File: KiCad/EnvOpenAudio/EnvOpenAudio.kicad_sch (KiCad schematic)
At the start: 65 parts, among them J1 USB_C_Receptacle_USB2.0, J2 Button, J5 Conn_01x03_Male, U1 TLV75533PDBV, U2 LM3880, U3 RP2040, U4 TLV320AIC3100, U5 TLV75518PDBV, U6 TLV75533PDBV, Y1 3225_4P 12MHz

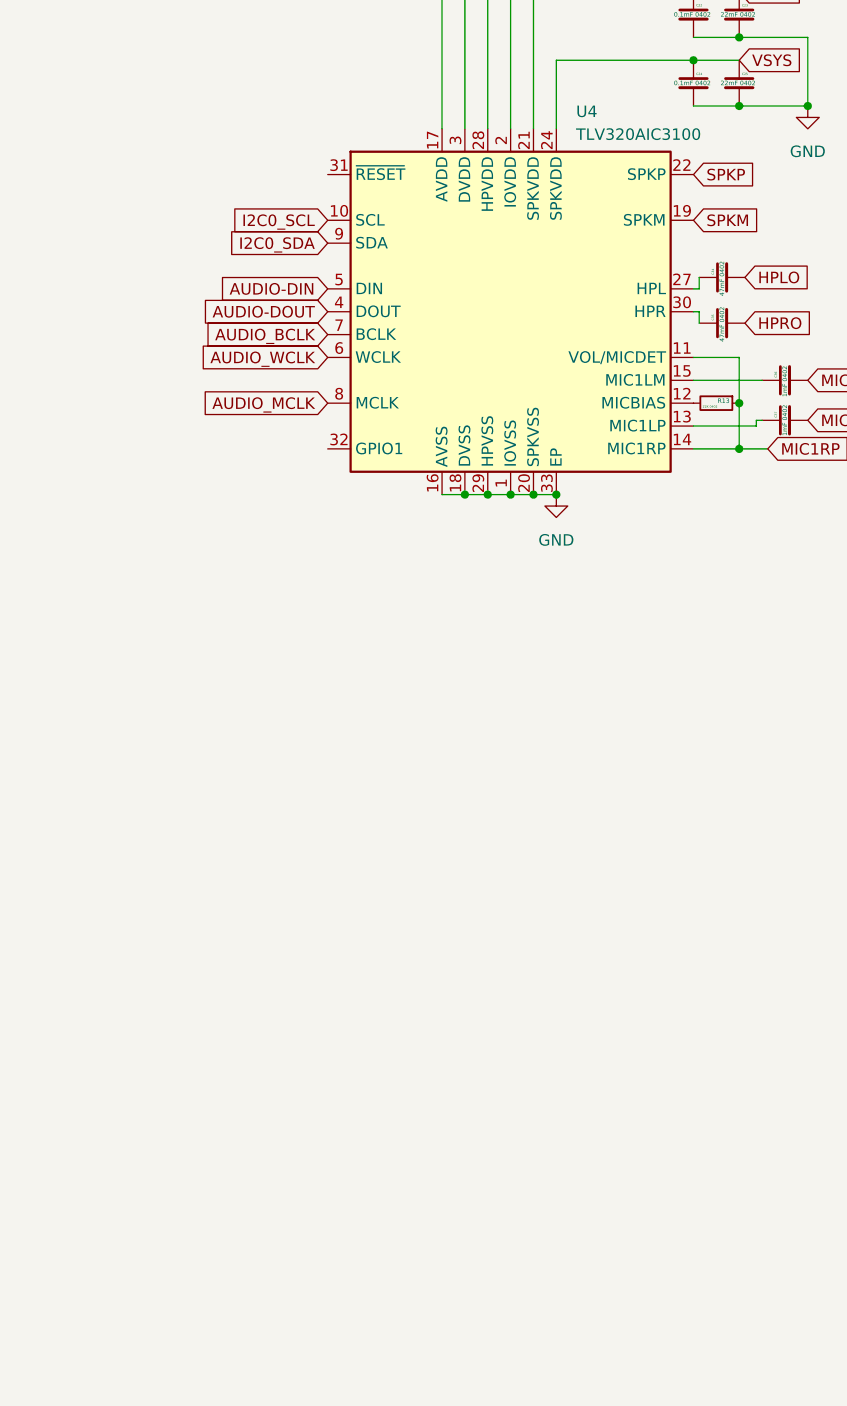
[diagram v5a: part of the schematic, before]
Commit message: wired up majority of PCB, added headers and labels.
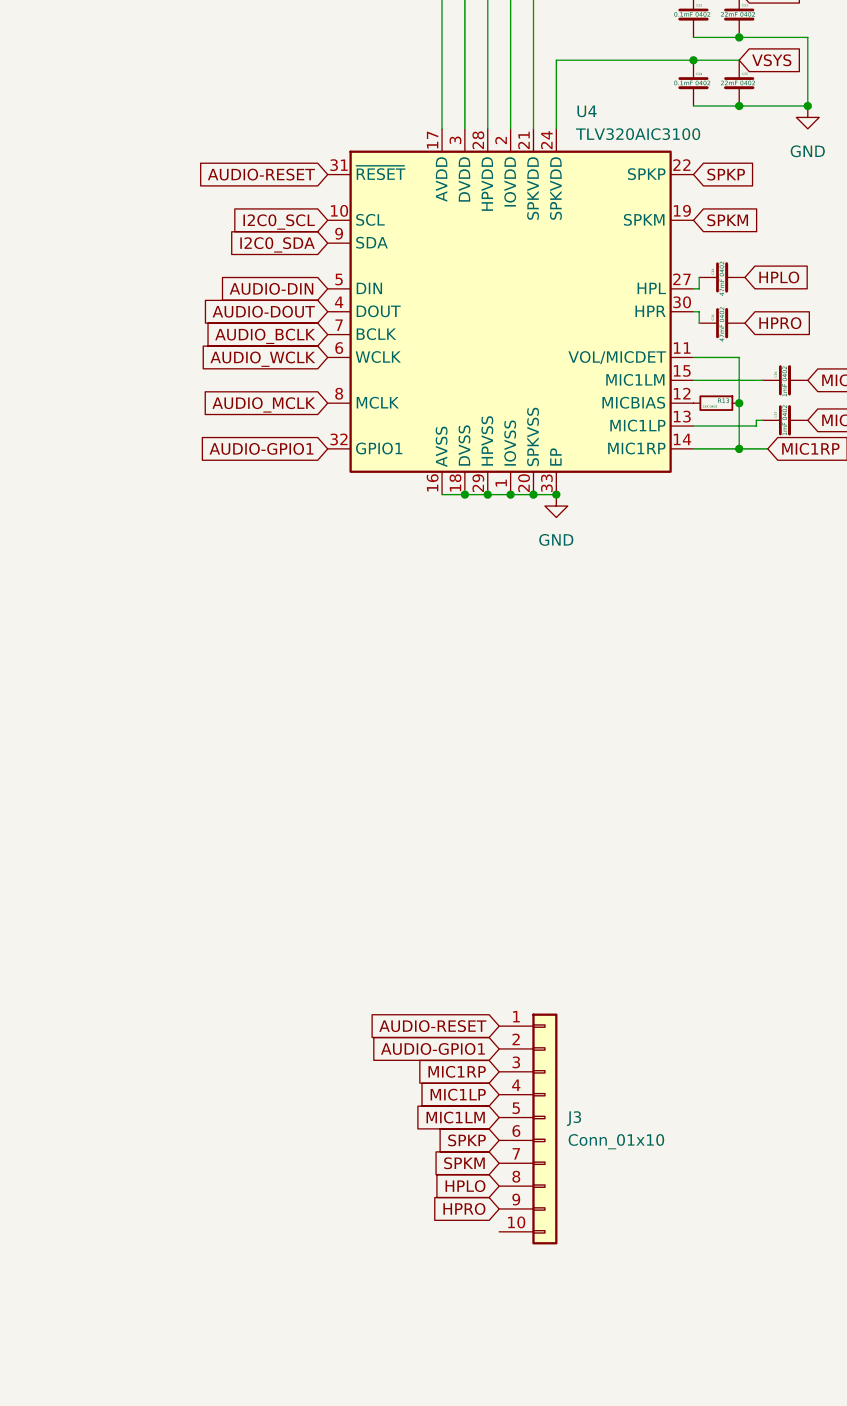
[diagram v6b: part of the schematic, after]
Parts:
- added J3: Conn_01x10, Connector_PinHeader_2.54mm:PinHeader_2x05_P2.54mm_Vertical, symbol Connector_Generic:Conn_01x10
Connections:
- net HPLO: now also J3.8 (Pin_8)
- net HPRO: now also J3.9 (Pin_9)
- net MIC1LM: now also J3.5 (Pin_5)
- net MIC1LP: now also J3.4 (Pin_4)
- net MIC1RP: now also J3.3 (Pin_3)
- net SPKM: now also J3.7 (Pin_7)
- net SPKP: now also J3.6 (Pin_6)
- net AUDIO-RESET: now reaches U4.31 (~{RESET})
- net AUDIO-RESET: now also J3.1 (Pin_1)
- net AUDIO-GPIO1: now reaches U4.32 (GPIO1)
- net AUDIO-GPIO1: now also J3.2 (Pin_2)
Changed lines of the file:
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@@
     (effects (font (size 1.27 1.27)) (justify right bottom))
   )
+  (global_label "AUDIO-RESET" (shape input) (at 311.15 186.055 180) (fields_autoplaced)
+    (effects (font (size 1.27 1.27)) (justify right))
+    (property "Intersheetrefs" "${INTERSHEET_REFS}" (at 295.8771 186.055 0)
+      (effects (font (size 1.27 1.27)) (justify right) hide)
+    )
+  )
   (global_label "USB_D-" (shape input) (at 43.18 34.925 0) (fields_autoplaced)
     (effects (font (size 1.27 1.27)) (justify left))
@@
     )
   )
+  (global_label "AUDIO-GPIO1" (shape input) (at 292.1 121.92 180) (fields_autoplaced)
+    (effects (font (size 1.27 1.27)) (justify right))
+    (property "Intersheetrefs" "${INTERSHEET_REFS}" (at 276.8874 121.92 0)
+      (effects (font (size 1.27 1.27)) (justify right) hide)
+    )
+  )
   (global_label "AUDIO_MCLK" (shape input) (at 292.1 116.84 180) (fields_autoplaced)
     (effects (font (size 1.27 1.27)) (justify right))
@@
     )
   )
+  (global_label "AUDIO-RESET" (shape input) (at 292.1 91.44 180) (fields_autoplaced)
+    (effects (font (size 1.27 1.27)) (justify right))
+    (property "Intersheetrefs" "${INTERSHEET_REFS}" (at 276.8271 91.44 0)
+      (effects (font (size 1.27 1.27)) (justify right) hide)
+    )
+  )
   (global_label "I2C0_SCL" (shape input) (at 292.1 96.52 180) (fields_autoplaced)
     (effects (font (size 1.27 1.27)) (justify right))
@@
     )
   )
+  (global_label "MIC1LM" (shape input) (at 311.15 196.215 180) (fields_autoplaced)
+    (effects (font (size 1.27 1.27)) (justify right))
+    (property "Intersheetrefs" "${INTERSHEET_REFS}" (at 301.8038 196.215 0)
+      (effects (font (size 1.27 1.27)) (justify right) hide)
+    )
+  )
   (global_label "AUDIO_MCLK" (shape input) (at 172.085 194.945 0) (fields_autoplaced)
     (effects (font (size 1.27 1.27)) (justify left))
@@
     )
   )
+  (global_label "MIC1RP" (shape input) (at 311.15 191.135 180) (fields_autoplaced)
+    (effects (font (size 1.27 1.27)) (justify right))
+    (property "Intersheetrefs" "${INTERSHEET_REFS}" (at 301.7433 191.135 0)
+      (effects (font (size 1.27 1.27)) (justify right) hide)
+    )
+  )
+  (global_label "MIC1LP" (shape input) (at 311.15 193.675 180) (fields_autoplaced)
+    (effects (font (size 1.27 1.27)) (justify right))
+    (property "Intersheetrefs" "${INTERSHEET_REFS}" (at 301.9852 193.675 0)
+      (effects (font (size 1.27 1.27)) (justify right) hide)
+    )
+  )
   (global_label "I2C0_SDA" (shape input) (at 172.085 189.865 0) (fields_autoplaced)
     (effects (font (size 1.27 1.27)) (justify left))
@@
     )
   )
+  (global_label "SPKM" (shape input) (at 311.15 201.295 180) (fields_autoplaced)
+    (effects (font (size 1.27 1.27)) (justify right))
+    (property "Intersheetrefs" "${INTERSHEET_REFS}" (at 303.6181 201.295 0)
+      (effects (font (size 1.27 1.27)) (justify right) hide)
+    )
+  )
   (global_label "VSYS" (shape input) (at 140.97 45.72 180) (fields_autoplaced)
     (effects (font (size 1.27 1.27)) (justify right))
@@
     )
   )
+  (global_label "HPLO" (shape input) (at 311.15 203.835 180) (fields_autoplaced)
+    (effects (font (size 1.27 1.27)) (justify right))
+    (property "Intersheetrefs" "${INTERSHEET_REFS}" (at 303.8599 203.835 0)
+      (effects (font (size 1.27 1.27)) (justify right) hide)
+    )
+  )
   (global_label "AUDIO_BCLK" (shape input) (at 292.1 109.22 180) (fields_autoplaced)
     (effects (font (size 1.27 1.27)) (justify right))
@@
     )
   )
+  (global_label "HPRO" (shape input) (at 311.15 206.375 180) (fields_autoplaced)
+    (effects (font (size 1.27 1.27)) (justify right))
+    (property "Intersheetrefs" "${INTERSHEET_REFS}" (at 303.618 206.375 0)
+      (effects (font (size 1.27 1.27)) (justify right) hide)
+    )
+  )
   (global_label "AUDIO-DIN" (shape input) (at 292.1 104.14 180) (fields_autoplaced)
     (effects (font (size 1.27 1.27)) (justify right))
@@
     )
   )
+  (global_label "AUDIO-GPIO1" (shape input) (at 311.15 188.595 180) (fields_autoplaced)
+    (effects (font (size 1.27 1.27)) (justify right))
+    (property "Intersheetrefs" "${INTERSHEET_REFS}" (at 295.9374 188.595 0)
+      (effects (font (size 1.27 1.27)) (justify right) hide)
+    )
+  )
   (global_label "AUDIO-DOUT" (shape input) (at 292.1 106.68 180) (fields_autoplaced)
     (effects (font (size 1.27 1.27)) (justify right))
@@
     (property "Intersheetrefs" "${INTERSHEET_REFS}" (at 344.7472 78.74 0)
       (effects (font (size 1.27 1.27)) (justify left) hide)
+    )
+  )
+  (global_label "SPKP" (shape input) (at 311.15 198.755 180) (fields_autoplaced)
+    (effects (font (size 1.27 1.27)) (justify right))
+    (property "Intersheetrefs" "${INTERSHEET_REFS}" (at 303.7995 198.755 0)
+      (effects (font (size 1.27 1.27)) (justify right) hide)
     )
   )
@@
         )
       )
+    )
+  )
+  (symbol (lib_id "Connector_Generic:Conn_01x10") (at 316.23 196.215 0) (unit 1)
+    (in_bom yes) (on_board yes) (dnp no) (fields_autoplaced)
+    (property "Reference" "J3" (at 318.77 196.215 0)
+      (effects (font (size 1.27 1.27)) (justify left))
+    )
+    (property "Value" "Conn_01x10" (at 318.77 198.755 0)
+      (effects (font (size 1.27 1.27)) (justify left))
+    )
+    (property "Footprint" "Connector_PinHeader_2.54mm:PinHeader_2x05_P2.54mm_Vertical" (at 316.23 196.215 0)
+      (effects (font (size 1.27 1.27)) hide)
+    )
+    (property "Datasheet" "~" (at 316.23 196.215 0)
+      (effects (font (size 1.27 1.27)) hide)
+    )
+    (pin "6")
+    (pin "10")
+    (pin "9")
+    (pin "3")
+    (pin "8")
+    (pin "4")
+    (pin "1")
+    (pin "5")
+    (pin "7")
+    (pin "2")
+    (instances
+      (project "EnvOpenAudio"
+        (path "/7b892ee5-f34f-4bca-8f87-a56522432f7c"
+          (reference "J3") (unit 1)
+        )
+      )

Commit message: Swapped RP2040 for RP2350A for FPU, re-did board and schematic, added labels back and naming, Github link
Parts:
- removed C1: 10uf 0402, Capacitor_SMD:C_0402_1005Metric, symbol Device:C
- removed C10: 2.2uF 0402, Capacitor_SMD:C_0402_1005Metric, symbol Device:C
- removed C16, C5, C6: 100nf 0402, Capacitor_SMD:C_0402_1005Metric, symbol Device:C
- removed C20, C21: 10uf 0402, Capacitor_SMD:C_0402_1005Metric, symbol Device:C_Small
- removed FLASH1: W25Q16JVUXIQ, Package_SON:SON-8-1EP_3x2mm_P0.5mm_EP1.4x1.6mm, symbol Memory_Flash:W25Q32JVZP
- removed J2: Button, Button_Switch_SMD:SW_SPST_B3U-1000P, symbol Switch:SW_Push
- removed J5: Conn_01x03_Male, Connector_PinHeader_1.00mm:PinHeader_1x03_P1.00mm_Vertical, symbol Connector_Generic:Conn_01x03
- removed R1: 1K 0402, Resistor_SMD:R_0402_1005Metric, symbol Device:R
- removed R12: 100K 0402, Resistor_SMD:R_0402_1005Metric, symbol Device:R_Small
- removed R4: 27r 0402 resistor, Resistor_SMD:R_0402_1005Metric, symbol Device:R
- removed RSW1: TSA343G00-250J2, Button_Switch_SMD:SW_SPST_B3U-1000P, symbol Switch:SW_Push
- removed U1, U6: TLV75533PDBV, Package_TO_SOT_SMD:SOT-23-5, symbol Regulator_Linear:TLV75533PDBV
- removed U3: RP2040, RP2040_minimal:RP2040-QFN-56, symbol MCU_RaspberryPi_RP2040:RP2040
- added C10, C5, C9: 10uF 0402, Capacitor_SMD:C_0402_1005Metric, symbol Device:C_Small
- added C20, C21, C22, C23: 100nf 0402, Capacitor_SMD:C_0402_1005Metric, symbol Device:C
- added C24: 10uf 0805, Capacitor_SMD:C_0805_2012Metric, symbol Device:C
- added C6: 0.1uF 0402, Capacitor_SMD:C_0402_1005Metric, symbol Device:C_Small
- added J2: SM03B-SRSS-TB, Connector_JST:JST_SH_SM03B-SRSS-TB_1x03-1MP_P1.00mm_Horizontal, symbol Connector_Generic_MountingPin:Conn_01x03_MountingPin
- added L1: SPH3015H2R2MT, Inductor_SMD:L_Sunlord_SWPA3015S, symbol Device:L_Small
- added L2: 3.3uf 2016, Inductor_SMD:L_Murata_DFE201610P, symbol Device:L
- added R10: 33r 0402, Resistor_SMD:R_0402_1005Metric, symbol Device:R
- added R13, R14: 27r 0402, Resistor_SMD:R_0402_1005Metric, symbol Device:R
- added R6: DNF, Resistor_SMD:R_0402_1005Metric, symbol Device:R
- added R8, R9: 1k 4020, Resistor_SMD:R_0402_1005Metric, symbol Device:R
- added SW1, SW2: B3U-1000, Button_Switch_SMD:SW_SPST_B3U-1000P-B, symbol Switch:SW_Push
- added U1: W25Q16JVUXIQ, Package_SON:SON-8-1EP_3x2mm_P0.5mm_EP1.4x1.6mm, symbol Memory_Flash:W25Q128JVS
- added U2: TPS63001DRCR, Package_SON:Texas_DRC0010J_ThermalVias, symbol Regulator_Switching:TPS63001
- added U4: RP2350_60QFN, RP2350_60QFN_minimal:RP2350-QFN-60-1EP_7x7_P0.4mm_EP3.4x3.4mm_ThermalVias, symbol MCU_RaspberryPi_RP2350:RP2350_60QFN
- C11, C15, C18: LCSC (none) -> (none)
- C13, C14: value 100nf 0402 -> 4.7uf 0402; LCSC (none) -> (none)
- C17, C4: value 10uf 0402 -> 100nf 0402; LCSC (none) -> (none)
- C19: value 22pf 0402 -> 100nf 0402; LCSC (none) -> (none)
- C2: value 22pf 0402 -> 15pf 0402; LCSC (none) -> (none)
- C3: value 1uf 0402 -> 15pf 0402; LCSC (none) -> (none)
- C7, C8: value 100nf 0402 -> 4.7uf 0402; footprint Capacitor_SMD:C_0402_1005Metric -> RP2350_60QFN_minimal:C_0402_1005Metric_small_pads; LCSC (none) -> (none)
- R11: value 1K 0402 -> 1k 4020; LCSC (none) -> (none)
- R2: value 10K 0402 -> DNF; LCSC (none) -> (none); now not fitted
- R3: value 27r 0402 resistor -> 0r 0402; LCSC (none) -> (none)
- R7: value 100K 0402 -> 100ohm 0402; LCSC (none) -> (none)
- U5: renamed from U4; footprint Package_DFN_QFN:VQFN-32-1EP_5x5mm_P0.5mm_EP3.5x3.5mm -> Package_DFN_QFN:VQFN-32-1EP_5x5mm_P0.5mm_EP3.15x3.15mm_ThermalVias
- Y1: value 3225_4P 12MHz -> ABM8-272-T3; LCSC (none) -> (none)
- renumbered C101 to C1, C9 to C12, C12 to C16, C32 to C25, C33 to C27, C30 to C28, C27 to C29, C28 to C30, C29 to C32, C22 to C33, C24 to C34, C34 to C35, C35 to C36, C23 to C37, C25 to C38, C36 to C39, C37 to C40, R102 to R1, R8 to R12, R13 to R15, R5 to R4, R6 to R5, U5 to U3, U2 to U6
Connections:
- net 3V3_EN is gone; now on net VSYS: R7.1
- net +1V1: now also C11.1, C14.1, C15.1, C8.1, L2.1, U4.23 (DVDD), U4.39 (DVDD), U4.50 (VREG_FB), U4.6 (DVDD); no longer C3.1, C7.1
- net +3V3: now also C19.1, C7.1, C10.1, C20.1, C21.1, C22.1, C23.1, C24.1, C9.1, R10.1, R6.1, U1.8 (VCC), U2.1 (VOUT), U2.10 (FB), U4.1 (IOVDD), U4.11 (IOVDD), U4.20 (IOVDD), U4.30 (IOVDD), U4.38 (IOVDD), U4.44 (ADC_AVDD), U4.45 (IOVDD), U4.49 (VREG_VIN), U4.53 (USB_OTP_VDD), U4.54 (QSPI_IOVDD); no longer C11.1, C13.1, C14.1, C15.1, C8.1, R2.1
- net AUDIO-DIN: now also U4.8 (GPIO5)
- net AUDIO-DOUT: now also U4.9 (GPIO6)
- net AUDIO_BCLK: now also U4.5 (GPIO3)
- net AUDIO_MCLK: now also U4.4 (GPIO2)
- net AUDIO_WCLK: now also U4.7 (GPIO4)
- net GND: now also C19.2, C2.2, C10.2, C20.2, C21.2, C22.2, C23.2, C24.2, C5.2, C6.2, C9.2, J2.2 (Pin_2), J2.MP (MountPin), R9.2, SW1.1, U1.4 (GND), U2.11 (PGND), U2.3 (PGND), U2.9 (GND), U4.47 (VREG_PGND), U4.61 (GND); no longer C19.1, C2.1
- net GPIO10: now also U4.14 (GPIO10)
- net GPIO11: now also U4.15 (GPIO11)
- net GPIO12: now also U4.16 (GPIO12)
- net GPIO13: now also U4.17 (GPIO13)
- net GPIO14: now also U4.18 (GPIO14)
- net GPIO15: now also U4.19 (GPIO15)
- net GPIO16: now also U4.27 (GPIO16)
- net GPIO17: now also U4.28 (GPIO17)
- net GPIO18: now also U4.29 (GPIO18)
- net GPIO19: now also U4.31 (GPIO19)
- net GPIO20: now also U4.32 (GPIO20)
- net GPIO21: now also U4.33 (GPIO21)
- net GPIO22: now also U4.34 (GPIO22)
- net GPIO23: now also U4.35 (GPIO23)
- net GPIO24: now also U4.36 (GPIO24)
- net GPIO25: now also U4.37 (GPIO25)
- net GPIO26_ADC0: now also U4.40 (GPIO26_ADC0)
- net GPIO27_ADC1: now also U4.41 (GPIO27_ADC1)
- net GPIO28_ADC2: now also U4.42 (GPIO28_ADC2)
- net GPIO29_ADC3: now also U4.43 (GPIO29_ADC3)
- net GPIO7: now also U4.10 (GPIO7)
- net GPIO8: now also U4.12 (GPIO8)
- net GPIO9: now also U4.13 (GPIO9)
- net I2C0_SCL: now also U4.3 (GPIO1)
- net I2C0_SDA: now also R2.1, U4.2 (GPIO0)
- net QSPI_SCLK: now also U1.6 (CLK), U4.56 (QSPI_SCLK)
- net QSPI_SD0: now also U1.5 (DI(IO0)), U4.57 (QSPI_SD0)
- net QSPI_SD1: now also U1.2 (DO(IO1)), U4.59 (QSPI_SD1)
- net QSPI_SD2: now also U1.3 (IO2), U4.58 (QSPI_SD2)
- net QSPI_SD3: now also U1.7 (IO3), U4.55 (QSPI_SD3)
- net QSPI_SS: now also R11.1, R3.1, U4.60 (QSPI_SS); no longer R2.2
- net RUN: now also SW2.2, U4.26 (RUN)
- net SWCLK: now also J2.1 (Pin_1), U4.24 (SWCLK)
- net SWD: now also J2.3 (Pin_3), U4.25 (SWD)
- net USB_D+: now also R13.1; no longer R3.1
- net USB_D-: now also R14.1
- net VSYS: now also C5.1, U2.5 (VIN); no longer R7.2
- net XIN: now also C2.1, U4.21 (XIN); no longer C2.2
- net XOUT: now also R8.1, U4.22 (XOUT); no longer R11.1
- net ~{USB_BOOT}: now also R11.2, SW1.2
- net FLASH_SS: now reaches R3.2
- net FLASH_SS: now also R2.2, R6.2, U1.1 (~{CS})
- new net: C6.1, R7.2, U2.6 (EN), U2.7 (PS/SYNC), U2.8 (VINA)
- new net: R13.2, U4.52 (USB_DP)
- new net: C3.1, R8.2, Y1.3
- new net: L1.1, U2.4 (L1)
- new net: L1.2, U2.2 (L2)
- new net: R14.2, U4.51 (USB_DM)
- new net: R9.1, SW2.1
- new net VREG_AVDD: C13.1, R10.2, U4.46 (VREG_AVDD)
- new net VREG_LX: L2.2, U4.48 (VREG_LX)
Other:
- note added: "12MHz Crystal"
- note added: "Flash"
- note added: "JST Debug Connector"
- note added: "Make sure R7 and R8 are close to RP2350"
- note removed: "Crystal"
- note removed: "Make sure C10 is close to pin 44 of RP2040"
- note removed: "SWAP FOR MORE POWERFUL 3V3 REGULATOR!"
- note removed: "These decoupling capacitors are meant to be put close by each 3.3V pin of the RP2040"
- moved on the sheet: C1, C12, C16, C25, C26, C27, C28, C29, C30, C31, C32, C33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

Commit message: added test pads, swapped inductors for smaller models
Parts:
- added TP1, TP2, TP3, TP4: TestPoint, TestPoint:TestPoint_Pad_D1.0mm, symbol Connector:TestPoint
- L1: value SPH3015H2R2MT -> MPL2016S2R2NHT; footprint Inductor_SMD:L_Sunlord_SWPA3015S -> Inductor_SMD:L_0805_2012Metric
- L2: value 3.3uf 2016 -> MPL2012S3R3MHT; footprint Inductor_SMD:L_Murata_DFE201610P -> Inductor_SMD:L_0805_2012Metric
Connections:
- net +3V3: now also TP4.1
- net VBUS: now also TP1.1
- net VSYS: now also TP2.1
